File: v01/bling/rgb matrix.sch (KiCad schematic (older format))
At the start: 76 parts, among them U3 IS31FL3733-TQ, U4 IS31FL3733-TQ

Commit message: Move RGB LED footprint to a local lib
I don't want as much content on the silkscreen.
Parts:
- D100, D101, D102, D103, D104, D105, D106, D107, D108, D55, D56, D57, D58, D59, D60, D61, D62, D63, D64, D65, D66, D67, D68, D69, D70, D71, D72, D73, D74, D75, D76, D77, D78, D79, D80, D81, D82, D83, D84, D85, D86, D87, D88, D89, D90, D91, D92, D93, D94, D95, D96, D97, D98, D99: footprint Keebio-Parts:RGB_3528_Blue_Notch-MX -> v01:RGB_3528_Blue_Notch-MX

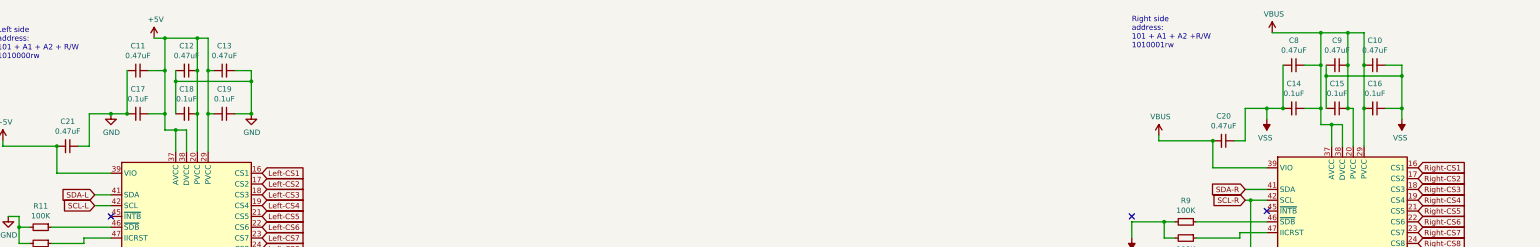
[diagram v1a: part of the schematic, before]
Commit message: Make schematic clearer
* Improve routing around mounting holes
* Fix all DRC errors.
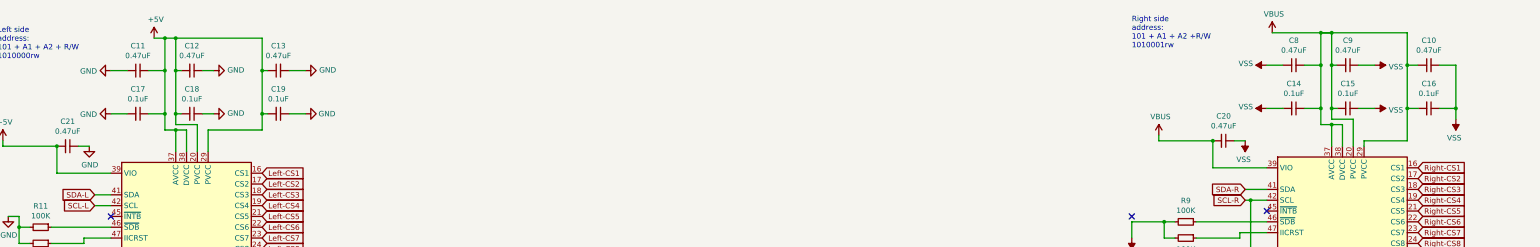
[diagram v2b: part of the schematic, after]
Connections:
- net +5V: now also C12.2, C18.2; no longer C12.1, C18.1
- net GND: now also C12.1, C18.1; no longer C12.2, C18.2
- net VBUS: now also C15.2, C9.2; no longer C15.1, C9.1
- net VSS: now also C15.1, C9.1; no longer C15.2, C9.2
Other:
- moved on the sheet: C10, C12, C13, C15, C16, C18, C19, C9

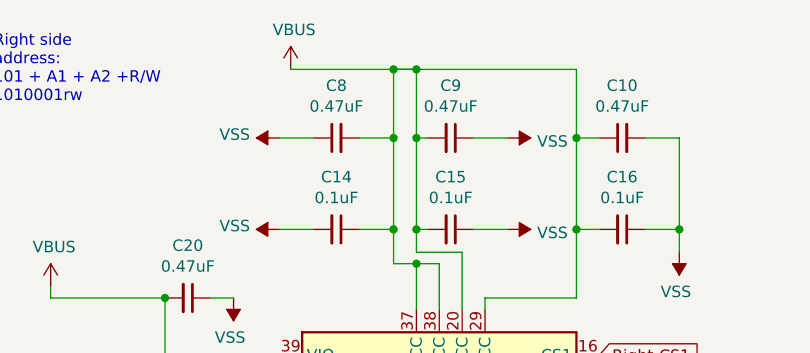
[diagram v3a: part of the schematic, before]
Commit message: Add ISP port to the bling board.
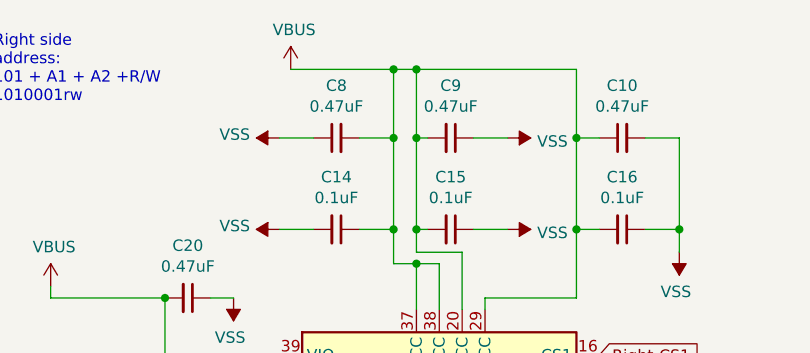
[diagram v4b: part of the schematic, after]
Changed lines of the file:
@@
 Wire Wire Line
 	13400 1800 13800 1800
-Wire Wire Line
-	13000 800  13100 800
 Connection ~ 13100 800
 Wire Wire Line

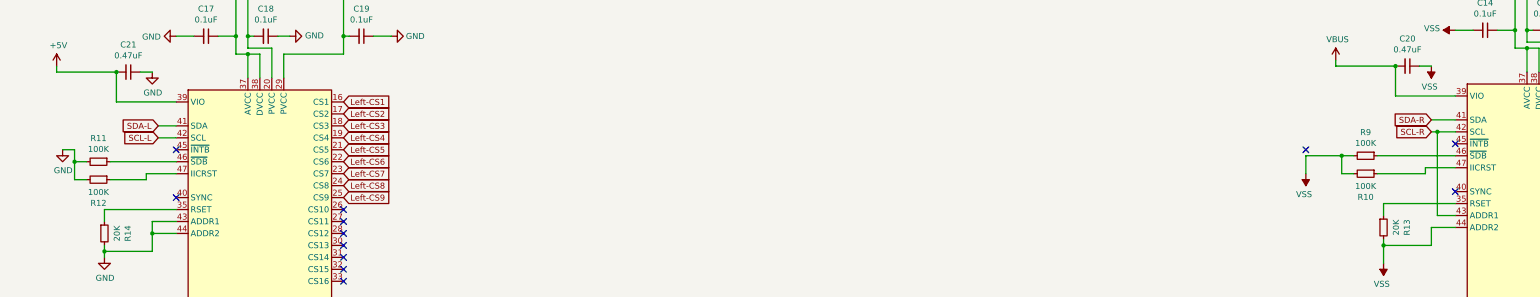
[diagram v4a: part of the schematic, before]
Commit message: Fix LED driver wiring
- Caps were not in ordered as per the docs. This doesn't matter *too*
  much but it is nice to be more correct.
- IS31FL3733 needs SDB set high to ensure the chip is always on.
  Previously it was pulled low causing the chip to shut off.
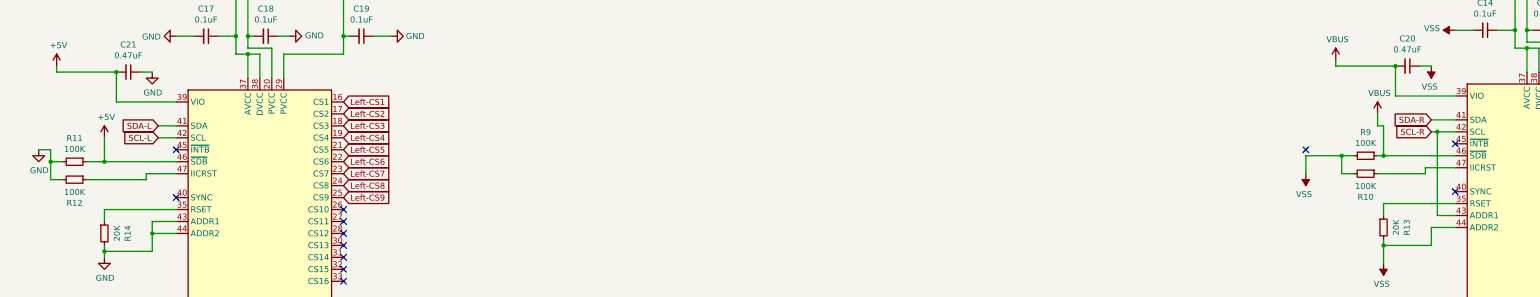
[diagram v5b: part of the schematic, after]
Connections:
- net +5V: now also R11.1, U4.46 (~SDB)
- net VBUS: now also R9.1, U3.46 (~SDB)
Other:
- moved on the sheet: R11, R12
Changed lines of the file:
@@
 L Device:R_Small R11
 U 1 1 612F67D0
-P 1150 2600
-F 0 "R11" V 954 2600 50  0000 C CNN
-F 1 "100K" V 1045 2600 50  0000 C CNN
-F 2 "Resistor_SMD:R_0805_2012Metric" H 1150 2600 50  0001 C CNN
-F 3 "~" H 1150 2600 50  0001 C CNN
-	1    1150 2600
-	0    1    1    0
-$EndComp
-Wire Wire Line
-	1050 2600 950  2600
+P 950 2600
+F 0 "R11" V 754 2600 50  0000 C CNN
+F 1 "100K" V 845 2600 50  0000 C CNN
+F 2 "Resistor_SMD:R_0805_2012Metric" H 950 2600 50  0001 C CNN
+F 3 "~" H 950 2600 50  0001 C CNN
+	1    950  2600
+	0    1    1    0
+$EndComp
+Wire Wire Line
+	850  2600 750  2600
 $Comp
 L Device:R_Small R12
 U 1 1 612F7594
-P 1150 2750
-F 0 "R12" V 1346 2750 50  0000 C CNN
-F 1 "100K" V 1255 2750 50  0000 C CNN
-F 2 "Resistor_SMD:R_0805_2012Metric" H 1150 2750 50  0001 C CNN
-F 3 "~" H 1150 2750 50  0001 C CNN
-	1    1150 2750
+P 950 2750
+F 0 "R12" V 1146 2750 50  0000 C CNN
+F 1 "100K" V 1055 2750 50  0000 C CNN
+F 2 "Resistor_SMD:R_0805_2012Metric" H 950 2750 50  0001 C CNN
+F 3 "~" H 950 2750 50  0001 C CNN
+	1    950  2750
 	0    1    1    0
 $EndComp
@@
 	1550 2700 1550 2750
 Wire Wire Line
-	1050 2750 950  2750
-Wire Wire Line
-	950  2500 950  2600
-Connection ~ 950  2600
+	850  2750 750  2750
+Wire Wire Line
+	750  2500 750  2600
+Connection ~ 750  2600
 $Comp
 L Device:R_Small R14
@@
 L power:GND #PWR0131
 U 1 1 6199C365
-P 850 2500
-F 0 "#PWR0131" H 850 2250 50  0001 C CNN
-F 1 "GND" H 855 2327 50  0000 C CNN
-F 2 "" H 850 2500 50  0001 C CNN
-F 3 "" H 850 2500 50  0001 C CNN
-	1    850  2500
+P 650 2500
+F 0 "#PWR0131" H 650 2250 50  0001 C CNN
+F 1 "GND" H 655 2327 50  0000 C CNN
+F 2 "" H 650 2500 50  0001 C CNN
+F 3 "" H 650 2500 50  0001 C CNN
+	1    650  2500
 	1    0    0    -1
 $EndComp
 Wire Wire Line
-	850  2500 950  2500
-Wire Wire Line
-	950  2600 950  2750
+	650  2500 750  2500
+Wire Wire Line
+	750  2600 750  2750
 Wire Wire Line
 	1200 3300 1200 3350
@@
 $EndComp
 Wire Wire Line
-	11850 2550 12500 2550
+	11850 2550 11900 2550
 Wire Wire Line
 	11850 2700 12250 2700
@@
 Wire Wire Line
 	1500 1850 1600 1850
-Wire Wire Line
-	1250 2600 1800 2600
-Wire Wire Line
-	1250 2750 1550 2750
 Wire Wire Line
 	12300 2250 12500 2250
@@
 Wire Wire Line
 	13100 800  13800 800
+Wire Wire Line
+	1050 2600 1200 2600
+Wire Wire Line
+	1050 2750 1550 2750
+$Comp
+L power:+5V #PWR?
+U 1 1 620D8D50
+P 1200 2400
+F 0 "#PWR?" H 1200 2250 50  0001 C CNN
+F 1 "+5V" H 1215 2573 50  0000 C CNN
+F 2 "" H 1200 2400 50  0001 C CNN
+F 3 "" H 1200 2400 50  0001 C CNN
+	1    1200 2400
+	1    0    0    -1
+$EndComp
+Wire Wire Line
+	1200 2400 1200 2600
+Connection ~ 1200 2600
+Wire Wire Line
+	1200 2600 1800 2600
+$Comp
+L power:VBUS #PWR?
+U 1 1 6212C89D
+P 11850 2200
+F 0 "#PWR?" H 11850 2050 50  0001 C CNN
+F 1 "VBUS" H 11865 2373 50  0000 C CNN
+F 2 "" H 11850 2200 50  0001 C CNN
+F 3 "" H 11850 2200 50  0001 C CNN
+	1    11850 2200
+	1    0    0    -1
+$EndComp
+Wire Wire Line
+	11850 2200 11850 2300
+Wire Wire Line
+	11850 2300 11900 2300
+Wire Wire Line
+	11900 2300 11900 2550
+Connection ~ 11900 2550
+Wire Wire Line
+	11900 2550 12500 2550
 $EndSCHEMATC
